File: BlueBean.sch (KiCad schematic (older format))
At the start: 1 part, among them U7 BLUE-BEAN

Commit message: started layout of the PCB, allso moved onto craken rum, from captin morgan. please for the love of god check the footprints are right. @MAX
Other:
- note added: "for blue tooth ??"
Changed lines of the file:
@@
 	1    0    0    -1
 $EndComp
+Text GLabel 3400 3100 0    50   BiDi ~ 0
+HOST1_DM
+Text GLabel 3400 3000 0    50   BiDi ~ 0
+HOST1_DP
+Text Notes 2850 2950 0    50   ~ 0
+for blue tooth ??
 $EndSCHEMATC

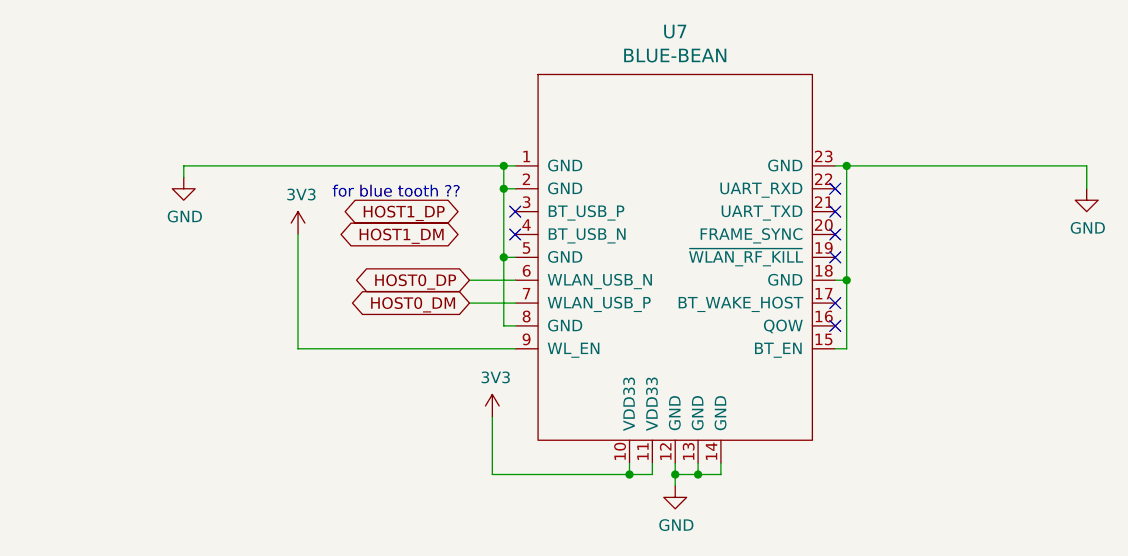
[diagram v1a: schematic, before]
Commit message: did some routing and fixed some pinouts on components
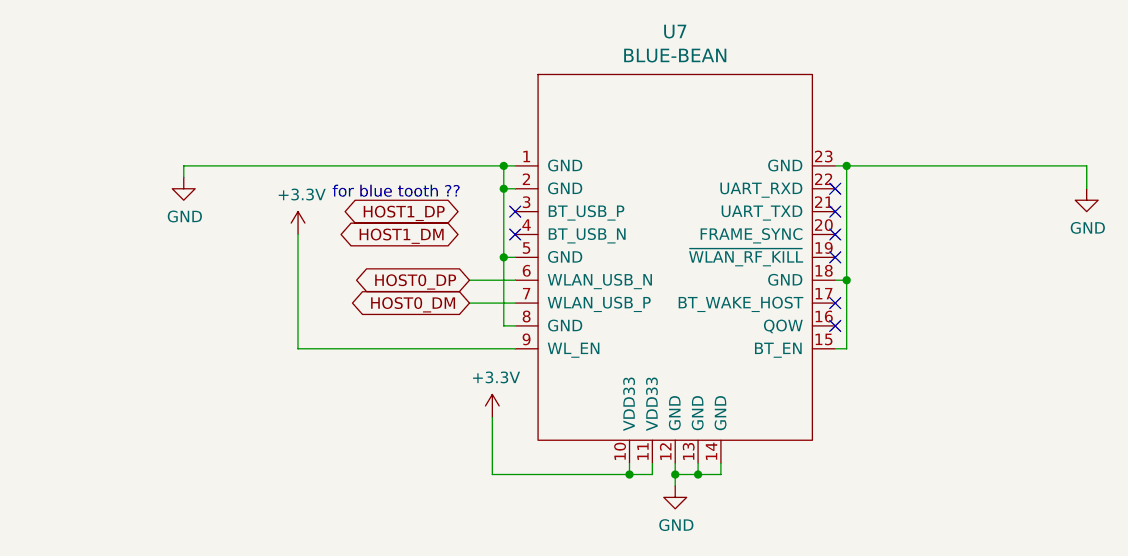
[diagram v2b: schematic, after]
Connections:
- net 3V3 renamed +3V3
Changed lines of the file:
@@
 	3550 4150 3550 3900
 Connection ~ 4150 4150
+Text GLabel 3400 3100 0    50   BiDi ~ 0
+HOST1_DM
+Text GLabel 3400 3000 0    50   BiDi ~ 0
+HOST1_DP
+Text Notes 2850 2950 0    50   ~ 0
+for blue tooth ??
 $Comp
-L Veo:3V3 #PWR0168
-U 1 1 5F57AB2F
+L power:+3.3V #PWR?
+U 1 1 604866DE
 P 3550 3900
+AR Path="/5F46881F/604866DE" Ref="#PWR?"  Part="1"
+AR Path="/5F56A00E/604866DE" Ref="#PWR0168"  Part="1"
 F 0 "#PWR0168" H 3550 3750 50  0001 C CNN
-F 1 "3V3" H 3565 4073 50  0000 C CNN
+F 1 "+3.3V" H 3565 4073 50  0000 C CNN
 F 2 "" H 3550 3900 50  0001 C CNN
 F 3 "" H 3550 3900 50  0001 C CNN
@@
 $EndComp
 $Comp
-L Veo:3V3 #PWR0169
-U 1 1 5F57B12F
+L power:+3.3V #PWR?
+U 1 1 604870BC
 P 2700 3100
+AR Path="/5F46881F/604870BC" Ref="#PWR?"  Part="1"
+AR Path="/5F56A00E/604870BC" Ref="#PWR0169"  Part="1"
 F 0 "#PWR0169" H 2700 2950 50  0001 C CNN
-F 1 "3V3" H 2715 3273 50  0000 C CNN
+F 1 "+3.3V" H 2715 3273 50  0000 C CNN
 F 2 "" H 2700 3100 50  0001 C CNN
 F 3 "" H 2700 3100 50  0001 C CNN
@@
 	1    0    0    -1
 $EndComp
-Text GLabel 3400 3100 0    50   BiDi ~ 0
-HOST1_DM
-Text GLabel 3400 3000 0    50   BiDi ~ 0
-HOST1_DP
-Text Notes 2850 2950 0    50   ~ 0
-for blue tooth ??
 $EndSCHEMATC

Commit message: added solder jumpers for optonla blue tooth
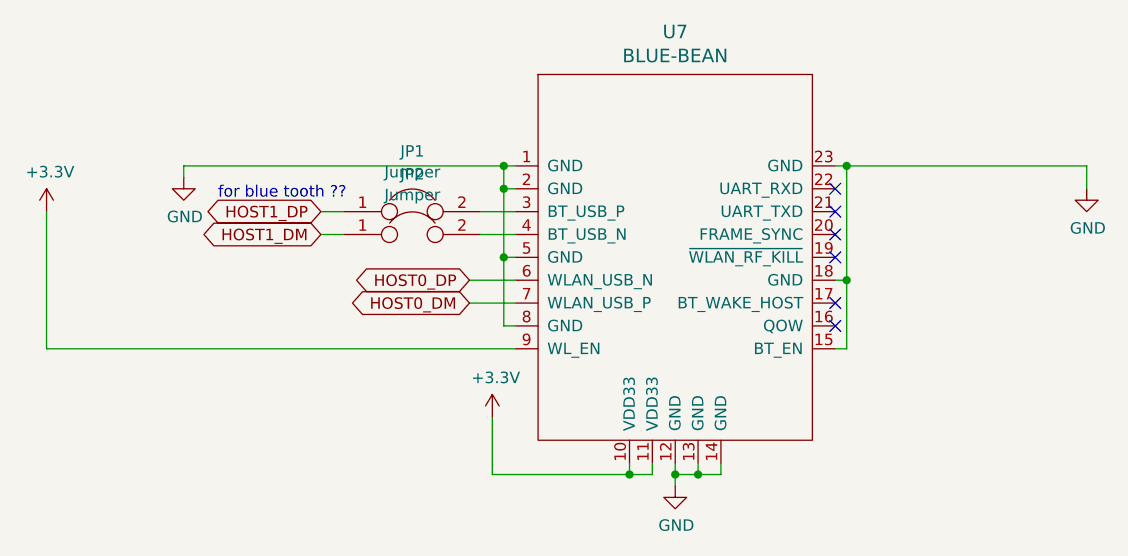
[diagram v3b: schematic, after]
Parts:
- added JP1, JP2: Jumper, Jumper:SolderJumper-2_P1.3mm_Open_TrianglePad1.0x1.5mm, symbol Device:Jumper
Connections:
- net HOST1_DM: now also JP2.1
- net HOST1_DP: now also JP1.1
- net at U7.3 (BT_USB_P): now also JP1.2
- net at U7.4 (BT_USB_N): now also JP2.2
- no-connect marks 8 -> 6
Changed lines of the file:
@@
 HOST0_DP
-$Comp
-L Veo:BLUE-BEAN U?
-U 1 1 5F56A572
-P 4350 3200
-AR Path="/5F529CC2/5F56A572" Ref="U?"  Part="1"
-AR Path="/5F56A00E/5F56A572" Ref="U7"  Part="1"
-F 0 "U7" H 4350 4186 59  0000 C CNN
-F 1 "BLUE-BEAN" H 4350 4081 59  0000 C CNN
-F 2 "Veo:BLUE-BEAN-A" H 4350 3200 118 0001 C CNN
-F 3 "https://www.8devices.com/media/products/bluebean/downloads/BLUE_bean_datasheet_v1.4-18-10-15.pdf" H 4350 2100 118 0001 C CNN
-	1    4350 3200
-	1    0    0    -1
-$EndComp
 $Comp
 L power:GND #PWR0165
@@
 Wire Wire Line
 	3450 3400 3650 3400
-NoConn ~ 3650 3100
-NoConn ~ 3650 3000
 NoConn ~ 5050 2900
 NoConn ~ 5050 3000
@@
 NoConn ~ 5050 3200
 Wire Wire Line
-	2700 3600 2700 3100
-Wire Wire Line
-	2700 3600 3650 3600
-Wire Wire Line
 	4250 4100 4250 4150
 Wire Wire Line
@@
 	3550 4150 3550 3900
 Connection ~ 4150 4150
-Text GLabel 3400 3100 0    50   BiDi ~ 0
+Text GLabel 2800 3100 0    50   BiDi ~ 0
 HOST1_DM
-Text GLabel 3400 3000 0    50   BiDi ~ 0
+Text GLabel 2800 3000 0    50   BiDi ~ 0
 HOST1_DP
-Text Notes 2850 2950 0    50   ~ 0
+Text Notes 2350 2950 0    50   ~ 0
 for blue tooth ??
 $Comp
@@
 L power:+3.3V #PWR?
 U 1 1 604870BC
-P 2700 3100
+P 1600 3000
 AR Path="/5F46881F/604870BC" Ref="#PWR?"  Part="1"
 AR Path="/5F56A00E/604870BC" Ref="#PWR0169"  Part="1"
-F 0 "#PWR0169" H 2700 2950 50  0001 C CNN
-F 1 "+3.3V" H 2715 3273 50  0000 C CNN
-F 2 "" H 2700 3100 50  0001 C CNN
-F 3 "" H 2700 3100 50  0001 C CNN
-	1    2700 3100
+F 0 "#PWR0169" H 1600 2850 50  0001 C CNN
+F 1 "+3.3V" H 1615 3173 50  0000 C CNN
+F 2 "" H 1600 3000 50  0001 C CNN
+F 3 "" H 1600 3000 50  0001 C CNN
+	1    1600 3000
 	1    0    0    -1
 $EndComp
+Wire Wire Line
+	1600 3000 1600 3600
+Wire Wire Line
+	1600 3600 3650 3600
+$Comp
+L Veo:BLUE-BEAN U?
+U 1 1 5F56A572
+P 4350 3200
+AR Path="/5F529CC2/5F56A572" Ref="U?"  Part="1"
+AR Path="/5F56A00E/5F56A572" Ref="U7"  Part="1"
+F 0 "U7" H 4350 4186 59  0000 C CNN
+F 1 "BLUE-BEAN" H 4350 4081 59  0000 C CNN
+F 2 "Veo:BLUE-BEAN-A" H 4350 3200 118 0001 C CNN
+F 3 "https://www.8devices.com/media/products/bluebean/downloads/BLUE_bean_datasheet_v1.4-18-10-15.pdf" H 4350 2100 118 0001 C CNN
+	1    4350 3200
+	1    0    0    -1
+$EndComp
+$Comp
+L Device:Jumper JP1
+U 1 1 607877C6
+P 3200 3000
+F 0 "JP1" H 3200 3264 50  0000 C CNN
+F 1 "Jumper" H 3200 3173 50  0000 C CNN
+F 2 "Jumper:SolderJumper-2_P1.3mm_Open_TrianglePad1.0x1.5mm" H 3200 3000 50  0001 C CNN
+F 3 "~" H 3200 3000 50  0001 C CNN
+	1    3200 3000
+	1    0    0    -1
+$EndComp
+$Comp
+L Device:Jumper JP2
+U 1 1 60788BBA
+P 3200 3100
+F 0 "JP2" H 3200 3364 50  0000 C CNN
+F 1 "Jumper" H 3200 3273 50  0000 C CNN
+F 2 "Jumper:SolderJumper-2_P1.3mm_Open_TrianglePad1.0x1.5mm" H 3200 3100 50  0001 C CNN
+F 3 "~" H 3200 3100 50  0001 C CNN
+	1    3200 3100
+	1    0    0    -1
+$EndComp
+Wire Wire Line
+	2900 3100 2800 3100
+Wire Wire Line
+	2800 3000 2900 3000
+Wire Wire Line
+	3500 3000 3650 3000
+Wire Wire Line
+	3650 3100 3500 3100
 $EndSCHEMATC
